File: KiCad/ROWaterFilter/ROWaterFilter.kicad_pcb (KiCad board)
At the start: 2 copper layers, 33 x 17.8 mm, 5 parts, among them J1 FTDI, J2 I2C, J3 Analog, J6 Analog, J7 Digital

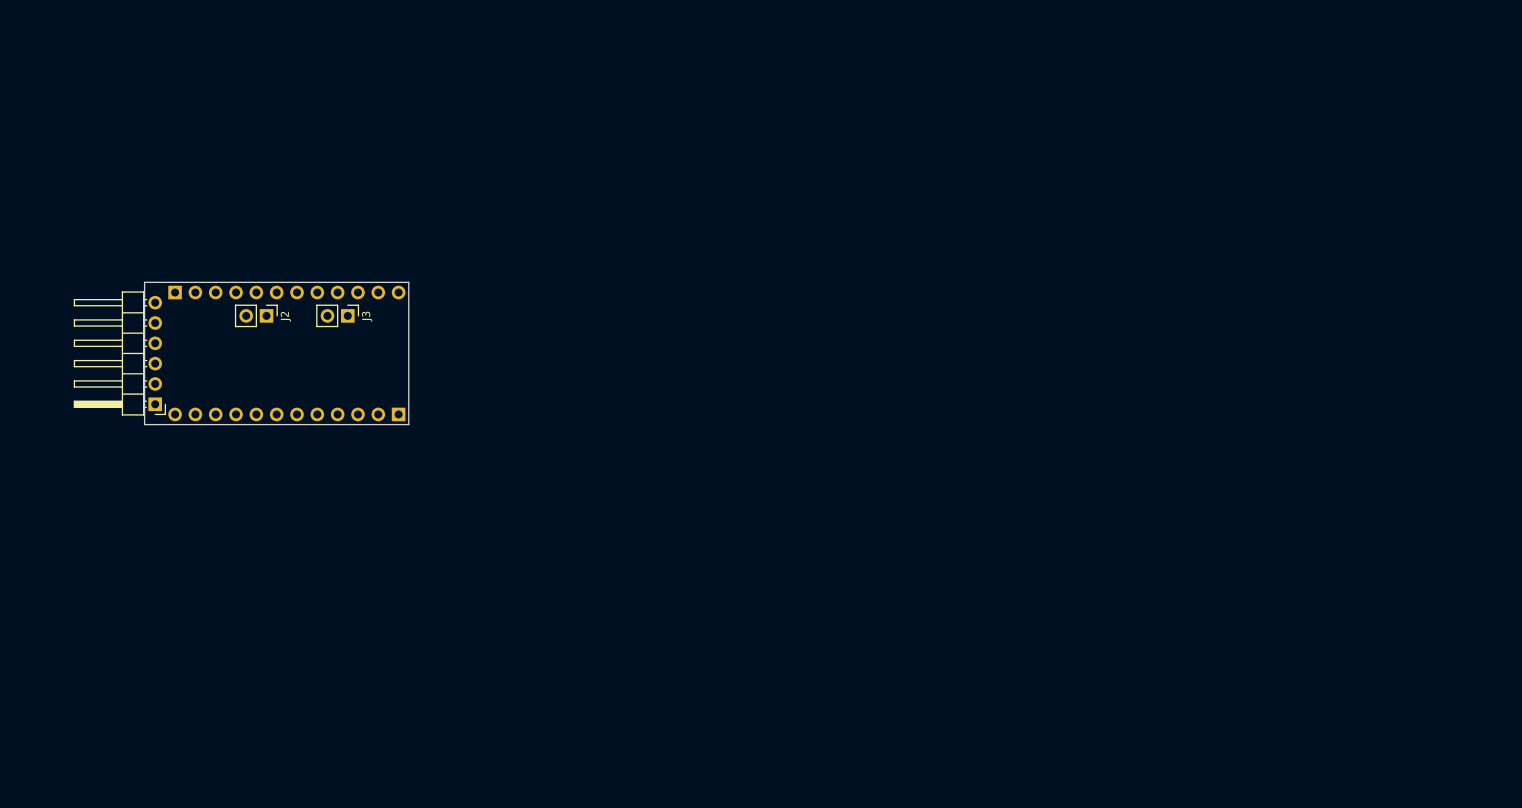
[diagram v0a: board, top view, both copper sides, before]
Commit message: docs, refactor, feat: readme update, refactor timers in lib, add time calibration function
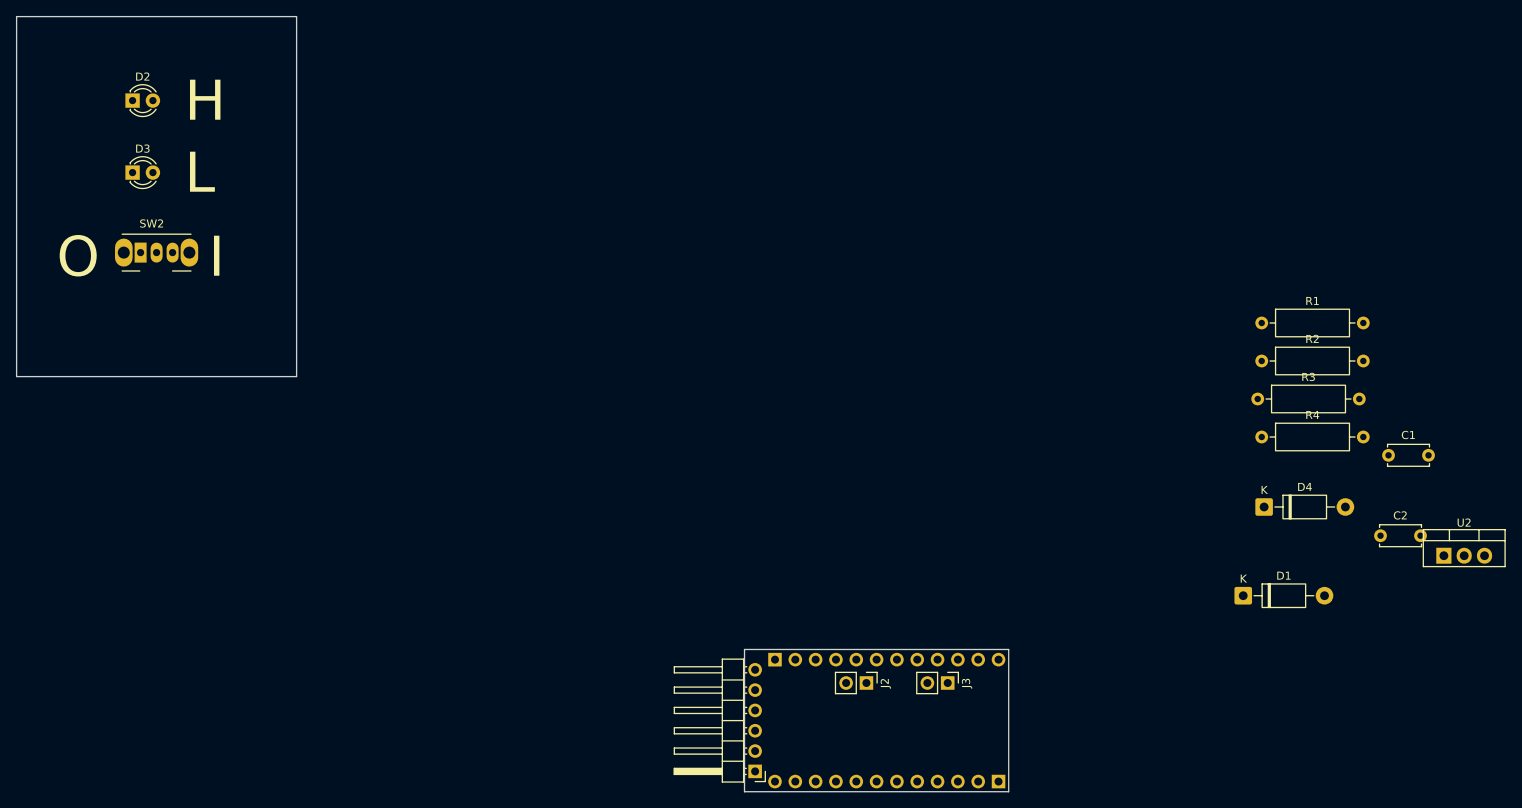
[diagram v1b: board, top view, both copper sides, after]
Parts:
- added C1: 0.33u, Capacitor_THT:C_Disc_D5.0mm_W2.5mm_P5.00mm, F.Cu at (255.5, 103.8)
- added C2: 0.1u, Capacitor_THT:C_Disc_D5.0mm_W2.5mm_P5.00mm, F.Cu at (254.5, 113.9)
- added D1: 1N4007, Diode_THT:D_DO-41_SOD81_P10.16mm_Horizontal, F.Cu at (237.3, 121.4)
- added D2: High P, LED_THT:LED_D3.0mm, F.Cu at (98.5, 59.5)
- added D3: Low P, LED_THT:LED_D3.0mm, F.Cu at (98.5, 68.5)
- added D4: 1N4007, Diode_THT:D_DO-41_SOD81_P10.16mm_Horizontal, F.Cu at (239.9, 110.3)
- added R1: 1k, Resistor_THT:R_Axial_DIN0309_L9.0mm_D3.2mm_P12.70mm_Horizontal, F.Cu at (239.6, 87.3)
- added R2: 1k, Resistor_THT:R_Axial_DIN0309_L9.0mm_D3.2mm_P12.70mm_Horizontal, F.Cu at (239.6, 92.0)
- added R3: 1k, Resistor_THT:R_Axial_DIN0309_L9.0mm_D3.2mm_P12.70mm_Horizontal, F.Cu at (239.1, 96.8)
- added R4: 10k, Resistor_THT:R_Axial_DIN0309_L9.0mm_D3.2mm_P12.70mm_Horizontal, F.Cu at (239.6, 101.5)
- added SW2: Maintenance mode switch, Button_Switch_THT:SW_Slide_SPDT_Angled_CK_OS102011MA1Q, F.Cu at (99.5, 78.5)
- added U2: L7805, Package_TO_SOT_THT:TO-220-3_Vertical, F.Cu at (262.4, 116.4)
- moved J1 87.9 mm to (176.3, 143.3)
- moved J6 87.9 mm to (178.8, 129.4)
- moved J7 87.9 mm to (206.7, 144.6)
- moved J2 87.9 mm to (190.2, 132.3)
- moved J3 87.9 mm to (200.4, 132.3)
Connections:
- J6 pad 1: VDC -> (no net)
- J6 pad 10: /MISO/D12 -> /SS/*D10
- J6 pad 11: /MOSI/*D11 -> (no net)
- J6 pad 12: /SS/*D10 -> (no net)
- J6 pad 2: GND -> (no net)
- J6 pad 3: /~{RESET} -> (no net)
- J6 pad 4: VCC -> (no net)
- J6 pad 5: /A3 -> (no net)
- J6 pad 6: /A2 -> (no net)
- J6 pad 7: /A1 -> (no net)
- J6 pad 8: /A0 -> (no net)
- J6 pad 9: /SCK/D13 -> (no net)
- J7 pad 1: /*D9 -> /TX
- J7 pad 10: /~{RESET} -> (no net)
- J7 pad 11: /RX -> (no net)
- J7 pad 12: /TX -> (no net)
- J7 pad 2: /D8 -> /D2
- J7 pad 3: /D7 -> /*D3
- J7 pad 4: /*D6 -> /D4
- J7 pad 6: /D4 -> /*D6
- J7 pad 7: /*D3 -> /D7
- J7 pad 8: /D2 -> /D8
- J7 pad 9: GND -> /*D9
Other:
- board size 33 x 17.8 mm -> 124 x 96.9 mm
- board text added: "H"
- board text added: "I"
- board text added: "L"
- board text added: "O"
